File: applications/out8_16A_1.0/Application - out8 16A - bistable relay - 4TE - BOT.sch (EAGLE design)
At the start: 29 parts, among them IC1 ULN2803, IC2 ULN2803, K1 HFE20-1-024-1HD504, K2 HFE20-1-024-1HD504, K3 HFE20-1-024-1HD504, K4 HFE20-1-024-1HD504, K5 HFE20-1-024-1HD504, K6 HFE20-1-024-1HD504, K7 HFE20-1-024-1HD504, K8 HFE20-1-024-1HD504

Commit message: renamed out8-V2 --> Application - out8 16A - bistable relay - 4TE - BOT
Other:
- note added: "2.0"
- note removed: "1.0"
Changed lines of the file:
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@@
 <?xml version="1.0" encoding="utf-8"?>
 <!DOCTYPE eagle SYSTEM "eagle.dtd">
-<eagle version="9.6.2">
+<eagle version="6.3">
 <drawing>
 <settings>
 <setting alwaysvectorfont="yes"/>
-<setting keepoldvectorfont="yes"/>
 <setting verticaltext="up"/>
 </settings>
@@
 <text x="-2.54" y="12.7" size="1.778" layer="91">- EIB</text>
 <text x="-5.08" y="25.4" size="1.778" layer="91">SMAJ40CA</text>
-<text x="237.49" y="-17.78" size="2.54" layer="100">1.0</text>
+<text x="237.49" y="-17.78" size="2.54" layer="100">2.0</text>
 <text x="149.86" y="5.08" size="3.81" layer="100">SB-out8 16A Applikation Board</text>
 <text x="149.86" y="0" size="2.54" layer="100">www.selfbus.org</text>

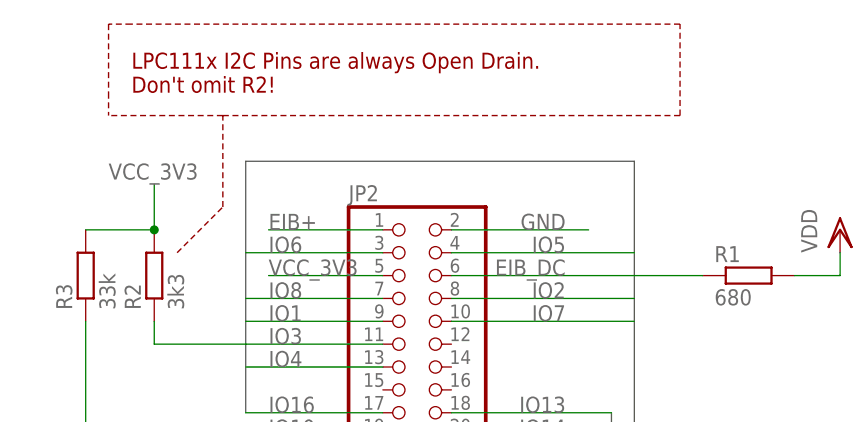
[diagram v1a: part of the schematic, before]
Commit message: renamed out8-V2.1 --> Application - out8 16A - bistable relay - 4TE - BOT
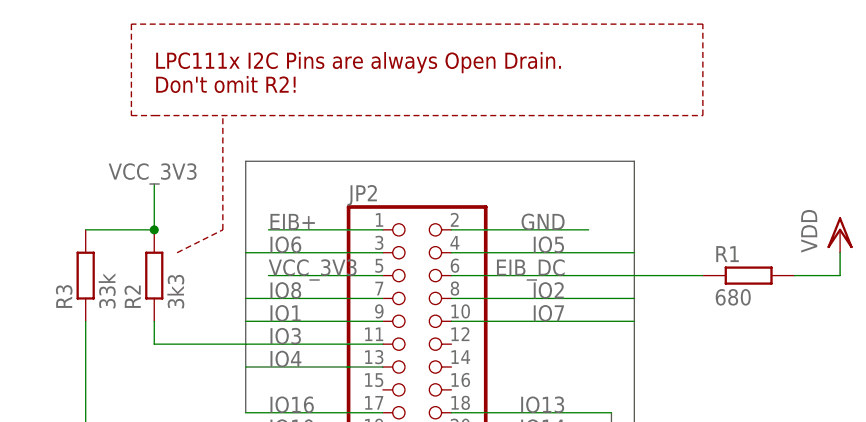
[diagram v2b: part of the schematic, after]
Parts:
- IC1, IC2: device uln-udn:ULN2803AADW -> uln-udn:ULN2803ASOP18
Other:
- note added: "2.1"
- note removed: "2.0"
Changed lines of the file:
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@@
 <part name="FRAME1" library="frames" deviceset="DINA4_L" device=""/>
 <part name="VDD2" library="supply1" deviceset="VDD" device=""/>
-<part name="IC1" library="uln-udn" deviceset="ULN2803A" device="ADW" value="ULN2803"/>
+<part name="IC1" library="uln-udn" deviceset="ULN2803A" device="SOP18" value="ULN2803"/>
 <part name="GND4" library="supply1" deviceset="GND" device=""/>
-<part name="IC2" library="uln-udn" deviceset="ULN2803A" device="ADW" value="ULN2803"/>
+<part name="IC2" library="uln-udn" deviceset="ULN2803A" device="SOP18" value="ULN2803"/>
 <part name="K2" library="sb-relay" deviceset="HFE20-1-024-1HD" device="504" value="HFE20-1-024-1HD504"/>
 <part name="K1" library="sb-relay" deviceset="HFE20-1-024-1HD" device="504" value="HFE20-1-024-1HD504"/>
@@
 <text x="-2.54" y="12.7" size="1.778" layer="91">- EIB</text>
 <text x="-5.08" y="25.4" size="1.778" layer="91">SMAJ40CA</text>
-<text x="237.49" y="-17.78" size="2.54" layer="100">2.0</text>
+<text x="237.49" y="-17.78" size="2.54" layer="100">2.1</text>
 <text x="149.86" y="5.08" size="3.81" layer="100">SB-out8 16A Applikation Board</text>
 <text x="149.86" y="0" size="2.54" layer="100">www.selfbus.org</text>
 <text x="185.42" y="-15.24" size="2.54" layer="100">Relais 8 x 230V / 16A </text>
-<text x="0" y="144.78" size="1.778" layer="94">LPC111x I2C Pins are always Open Drain.
+<text x="2.54" y="144.78" size="1.778" layer="94">LPC111x I2C Pins are always Open Drain.
 Don't omit R2!</text>
-<wire x1="5.08" y1="127" x2="10.16" y2="132.08" width="0.1524" layer="94" style="shortdash"/>
-<wire x1="10.16" y1="132.08" x2="10.16" y2="142.24" width="0.1524" layer="94" style="shortdash"/>
-<wire x1="10.16" y1="142.24" x2="-2.54" y2="142.24" width="0.1524" layer="94" style="shortdash"/>
-<wire x1="10.16" y1="142.24" x2="60.96" y2="142.24" width="0.1524" layer="94" style="shortdash"/>
-<wire x1="60.96" y1="142.24" x2="60.96" y2="152.4" width="0.1524" layer="94" style="shortdash"/>
-<wire x1="60.96" y1="152.4" x2="0" y2="152.4" width="0.1524" layer="94" style="shortdash"/>
-<wire x1="0" y1="152.4" x2="-2.54" y2="152.4" width="0.1524" layer="94" style="shortdash"/>
-<wire x1="-2.54" y1="152.4" x2="-2.54" y2="144.78" width="0.1524" layer="94" style="shortdash"/>
-<wire x1="-2.54" y1="144.78" x2="-2.54" y2="142.24" width="0.1524" layer="94" style="shortdash"/>
+<wire x1="5.08" y1="127" x2="10.16" y2="129.54" width="0.1524" layer="94" style="shortdash"/>
+<wire x1="10.16" y1="129.54" x2="10.16" y2="142.24" width="0.1524" layer="94" style="shortdash"/>
+<wire x1="2.54" y1="142.24" x2="63.5" y2="142.24" width="0.1524" layer="94" style="shortdash"/>
+<wire x1="63.5" y1="142.24" x2="63.5" y2="152.4" width="0.1524" layer="94" style="shortdash"/>
+<wire x1="63.5" y1="152.4" x2="0" y2="152.4" width="0.1524" layer="94" style="shortdash"/>
+<wire x1="0" y1="152.4" x2="0" y2="142.24" width="0.1524" layer="94" style="shortdash"/>
+<wire x1="0" y1="142.24" x2="2.54" y2="142.24" width="0.1524" layer="94" style="shortdash"/>
 </plain>
 <instances>

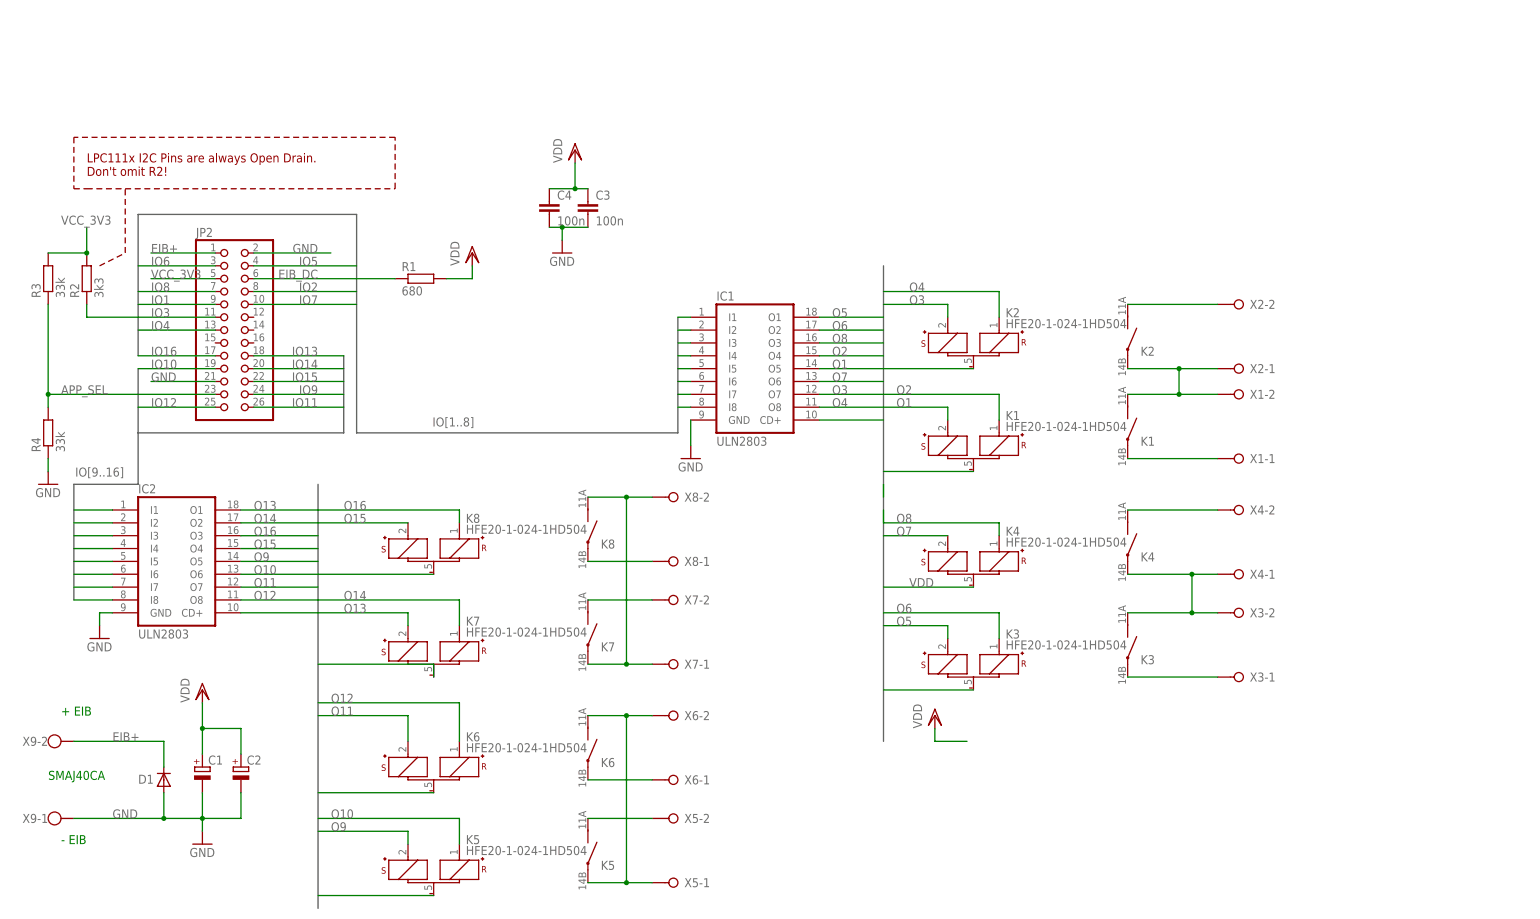
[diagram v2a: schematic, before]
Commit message: updated Application - out8 16A - bistable relay - 4TE - BOT - V2.2; added SJ2 for use with addon - energy storage; opütimized silkscreen and relaypositions
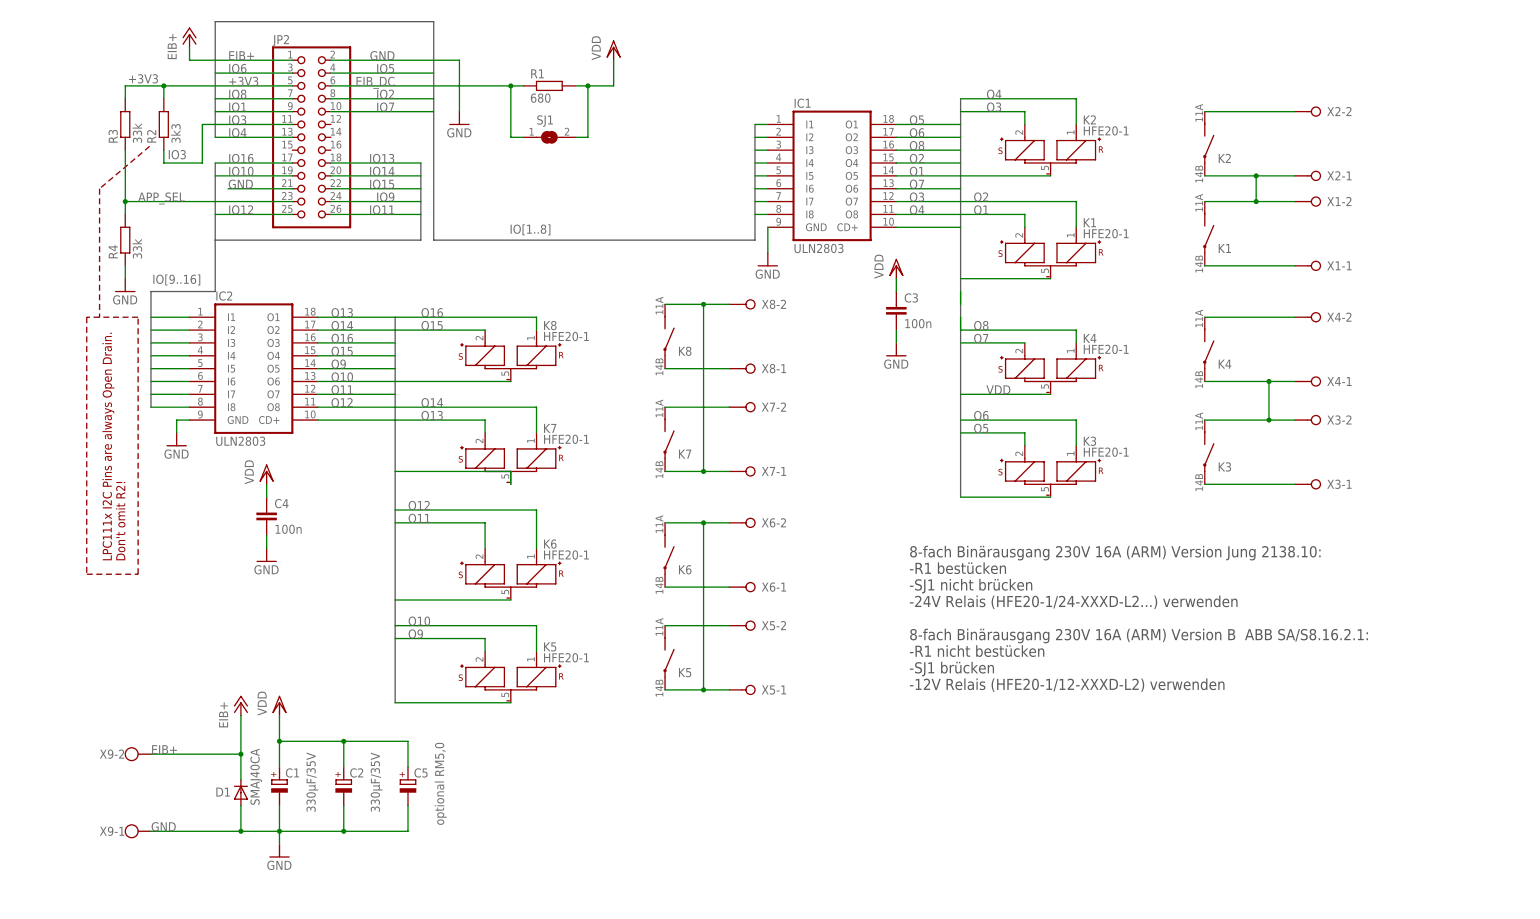
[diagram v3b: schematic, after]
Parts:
- added C5: optional RM5,0, rcl:CPOL-EUE5-13
- added SJ1: (no value), jumper:SJ
- C1, C2: value (none) -> 330µF/35V
- D1: value (none) -> SMAJ40CA
- K1, K2, K3, K4, K5, K6, K7, K8: value HFE20-1-024-1HD504 -> HFE20-1
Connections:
- net VCC_3V3 renamed +3V3
- net EIB_DC: now also SJ1.1
- net GND: now also C5.-
- net VDD: now also C5.+, SJ1.2
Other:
- note added: "2.2"
- note added: "8-fach Binärausgang 230V 16A (ARM) Version Jung 2138.10: -R1 bestücken -SJ1 nicht brücken -24V Relais (HFE20-1/24-XXXD-L2...) verwenden 8-fach Binärausgang 230V 16A (ARM) Version B ABB SA/S8.16.2.1: -R1 nicht bestücken -SJ1 brücken -12V Relais (HFE20-1/12-XXXD-L2) verwenden"
- note added: "out8 16A Application Board"
- note removed: "+ EIB"
- note removed: "- EIB"
- note removed: "2.1"
- note removed: "SB-out8 16A Applikation Board"
- note removed: "SMAJ40CA"
- moved on the sheet: C1, C2, C3, C4, D1, IC1, IC2, JP2, K1, K2, K3, K4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

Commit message: C5 entfernt Polygone eingefügt
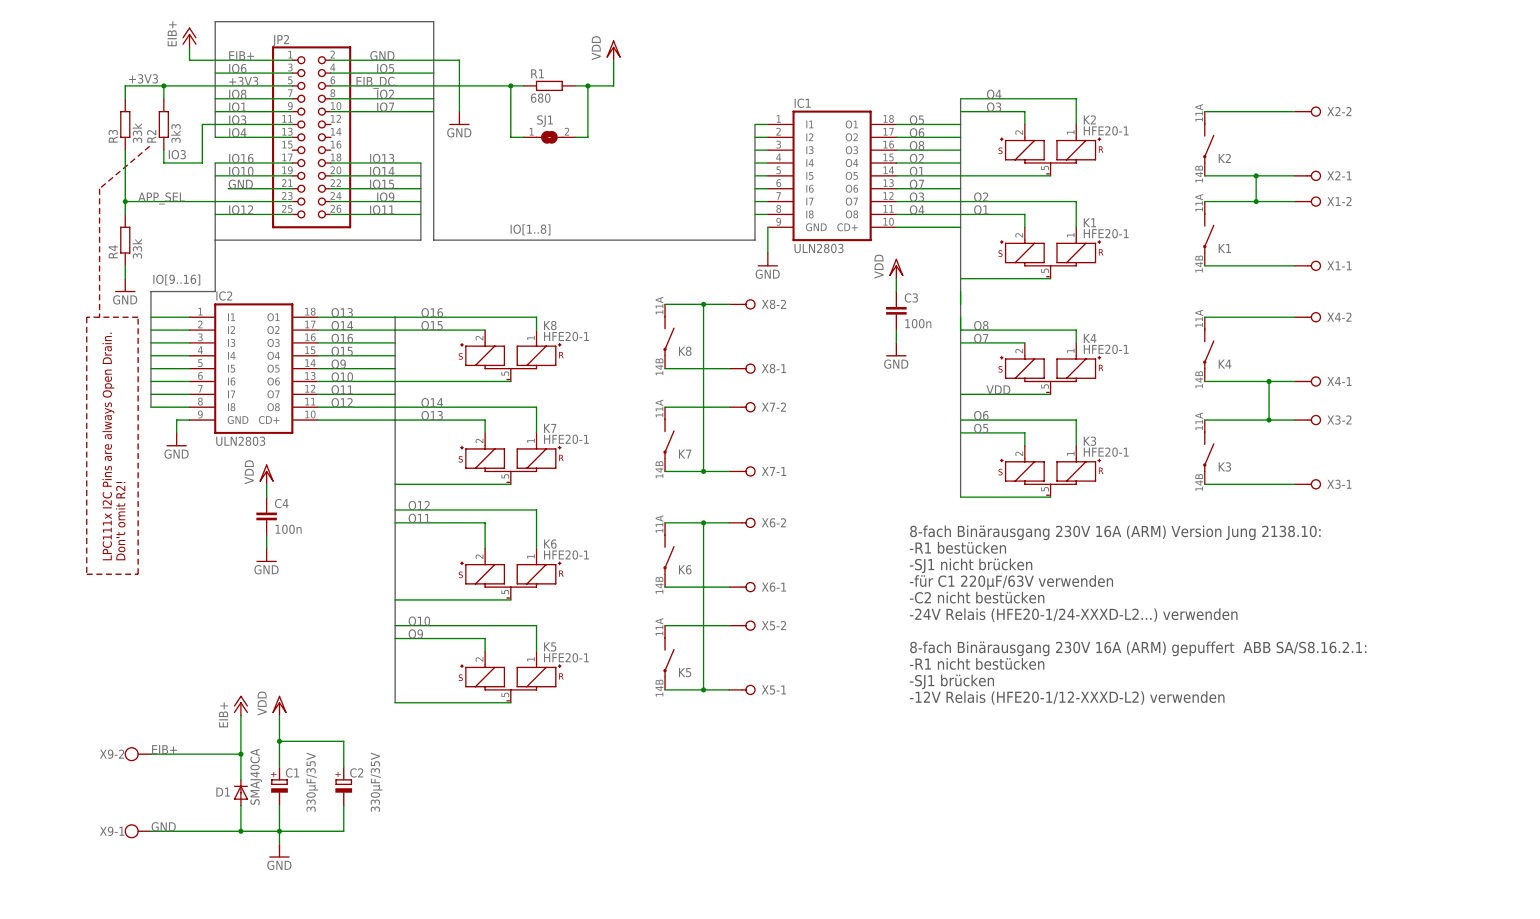
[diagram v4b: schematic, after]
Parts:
- removed C5: optional RM5,0, rcl:CPOL-EUE5-13
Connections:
- net GND: no longer C5.-
- net VDD: no longer C5.+
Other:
- note added: "8-fach Binärausgang 230V 16A (ARM) Version Jung 2138.10: -R1 bestücken -SJ1 nicht brücken -für C1 220µF/63V verwenden -C2 nicht bestücken -24V Relais (HFE20-1/24-XXXD-L2...) verwenden 8-fach Binärausgang 230V 16A (ARM) gepuffert ABB SA/S8.16.2.1: -R1 nicht bestücken -SJ1 brücken -12V Relais (HFE20-1/12-XXXD-L2) verwenden"
- note removed: "8-fach Binärausgang 230V 16A (ARM) Version Jung 2138.10: -R1 bestücken -SJ1 nicht brücken -24V Relais (HFE20-1/24-XXXD-L2...) verwenden 8-fach Binärausgang 230V 16A (ARM) Version B ABB SA/S8.16.2.1: -R1 nicht bestücken -SJ1 brücken -12V Relais (HFE20-1/12-XXXD-L2) verwenden"
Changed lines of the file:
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@@
 <part name="VDD5" library="supply1" deviceset="VDD" device=""/>
 <part name="GND6" library="supply1" deviceset="GND" device=""/>
-<part name="C5" library="rcl" deviceset="CPOL-EU" device="E5-13" value="optional RM5,0"/>
 <part name="GND7" library="supply1" deviceset="GND" device=""/>
 <part name="P+1" library="supply1" deviceset="+12V" device="" value="EIB+"/>
@@
 <text x="167.64" y="25.4" size="2.54" layer="100">www.selfbus.org</text>
 <text x="203.2" y="10.16" size="2.54" layer="100">Relais 8 x 230V / 16A </text>
-<text x="165.1" y="43.18" size="2.1844" layer="97">8-fach Binärausgang 230V 16A (ARM) Version Jung 2138.10:
+<text x="165.1" y="40.64" size="2.1844" layer="97">8-fach Binärausgang 230V 16A (ARM) Version Jung 2138.10:
 -R1 bestücken
 -SJ1 nicht brücken
+-für C1 220µF/63V verwenden
+-C2 nicht bestücken
 -24V Relais (HFE20-1/24-XXXD-L2...) verwenden
-8-fach Binärausgang 230V 16A (ARM) Version B  ABB SA/S8.16.2.1:
+8-fach Binärausgang 230V 16A (ARM) gepuffert  ABB SA/S8.16.2.1:
 -R1 nicht bestücken
 -SJ1 brücken
@@
 <instance part="VDD5" gate="G$1" x="38.1" y="86.36"/>
 <instance part="GND6" gate="1" x="38.1" y="68.58"/>
-<instance part="C5" gate="G$1" x="66.04" y="25.4" smashed="yes">
-<attribute name="NAME" x="67.183" y="25.8826" size="1.778" layer="95"/>
-<attribute name="VALUE" x="73.1774" y="16.383" size="1.778" layer="96" rot="R90"/>
-</instance>
 <instance part="GND7" gate="1" x="76.2" y="154.94"/>
 <instance part="P+1" gate="1" x="22.86" y="172.72" smashed="yes">
-<attribute name="VALUE" x="20.32" y="167.64" size="1.778" layer="96" rot="R90"/>
+<attribute name="VALUE" x="20.32" y="170.18" size="1.778" layer="96" rot="R90"/>
 </instance>
 <instance part="P+2" gate="1" x="33.02" y="40.64" smashed="yes">
@@
 <wire x1="40.64" y1="15.24" x2="53.34" y2="15.24" width="0.1524" layer="91"/>
 <wire x1="53.34" y1="15.24" x2="53.34" y2="20.32" width="0.1524" layer="91"/>
-<pinref part="C5" gate="G$1" pin="-"/>
-<wire x1="66.04" y1="20.32" x2="66.04" y2="15.24" width="0.1524" layer="91"/>
-<wire x1="66.04" y1="15.24" x2="53.34" y2="15.24" width="0.1524" layer="91"/>
-<junction x="53.34" y="15.24"/>
 </segment>
 <segment>
@@
 <wire x1="53.34" y1="33.02" x2="40.64" y2="33.02" width="0.1524" layer="91"/>
 <junction x="40.64" y="33.02"/>
-<pinref part="C5" gate="G$1" pin="+"/>
-<wire x1="53.34" y1="33.02" x2="66.04" y2="33.02" width="0.1524" layer="91"/>
-<wire x1="66.04" y1="33.02" x2="66.04" y2="27.94" width="0.1524" layer="91"/>
-<junction x="53.34" y="33.02"/>
 </segment>
 <segment>
@@
 </segment>
 <segment>
-<wire x1="86.36" y1="83.82" x2="86.36" y2="86.36" width="0.1524" layer="91"/>
-<wire x1="86.36" y1="86.36" x2="63.5" y2="86.36" width="0.1524" layer="91"/>
+<wire x1="86.36" y1="83.82" x2="63.5" y2="83.82" width="0.1524" layer="91"/>
 <pinref part="K7" gate="G$1" pin="-"/>
 </segment>
